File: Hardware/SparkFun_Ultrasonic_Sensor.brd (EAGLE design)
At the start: 45 x 21.5 mm, 51 parts, among them J2 BM04B-SRSS-TB, J3 BM04B-SRSS-TB, Q1 847, U2 STM8L051, U3 TCT40-16T, U4 TCT40-16R, U6 LMV324

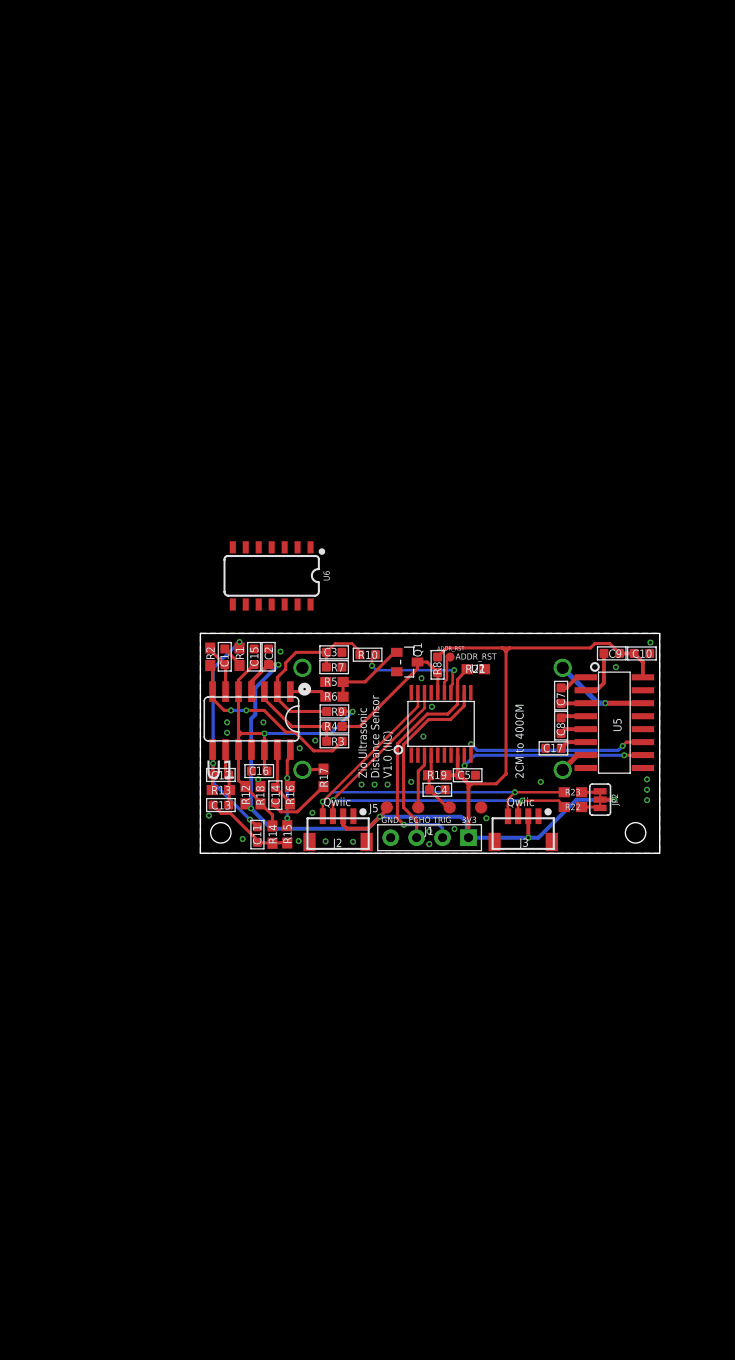
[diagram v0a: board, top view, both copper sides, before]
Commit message: Removes almost any lingering parts from old design. Gets close to finishing schematic
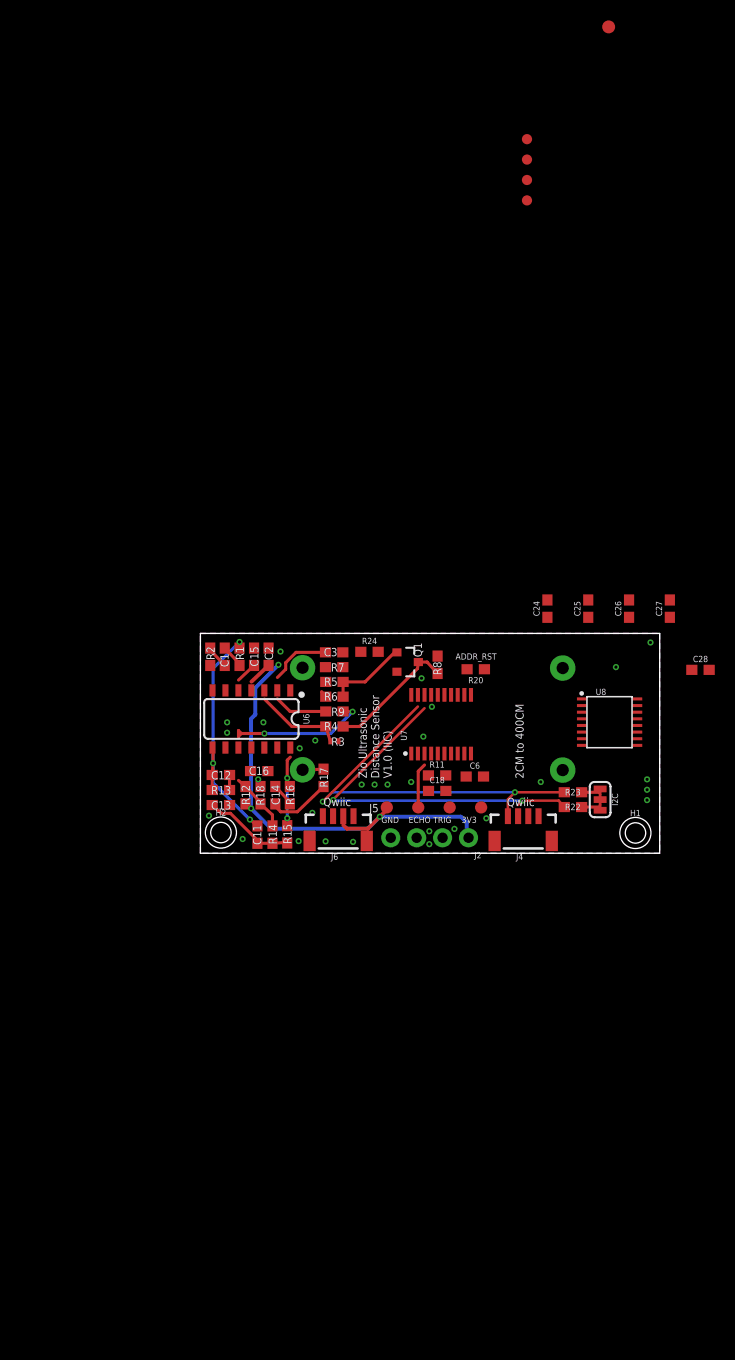
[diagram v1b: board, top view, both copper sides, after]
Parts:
- removed ADDR_RST: (no value), Connector:1P-35MIL
- removed C10, C17, C7, C8, C9: 1uF ±10% 50V, Discretex:0603
- removed C4, C5: 100nF ±10% 50V, Discretex:0603
- removed J1: (no value), Connector:4P-65/35MIL
- removed J3: BM04B-SRSS-TB, Connector:JST-SH-4P-90
- removed JP2: SMT-JUMPER_3_2-NC_TRACE, NOA-Jumpers:SMT-JUMPER_3_2-NC_TRACE
- removed R10: 100K ±1%, Discretex:0603
- removed R19, R21: 10k, SparkFun-Resistors:0603
- removed U1: (no value), IC:SO014
- removed U2: STM8L051, IC:TSSOP20
- removed U3: TCT40-16T, Discretex:TCT40-16T/R
- removed U4: TCT40-16R, Discretex:TCT40-16T/R
- added C18, C24, C25, C26, C27, C28, C6: 0.1uF, SparkFun-Capacitors:0603
- added FD1, FD2, FD3, FD4: FIDUCIAL1X2, SparkFun-Aesthetics:FIDUCIAL-1X2
- added FRAME1: FRAME-LEDGER, SparkFun-Aesthetics:CREATIVE_COMMONS
- added H1, H2: STAND-OFFTIGHT, SparkFun-Hardware:STAND-OFF-TIGHT
- added I2C: JUMPER-SMT_3_2-NC_TRACE_SILK, SparkFun-Jumpers:SMT-JUMPER_3_2-NC_TRACE_SILK
- added J4, J6: Vertical Qwiic Connector, SparkFun-Connectors:JST04_1MM_VERT
- added R11, R20: 10k, SparkFun-Resistors:0603
- added R24: 100k, SparkFun-Resistors:0603
- added TP1: TEST-POINT3X5, SparkFun-Connectors:PAD.03X.05
- added U7: STM8L051F3, new_parts:TSSOP20
- added U8: SP3232EB, new_parts:TSSOP16
- added U9: ULTRASONIC_SENSOR_RECEIVER, new_parts:CUSA-R80
- C1, C14: value 10nF ±10% 50V -> 10nF; device Discretex:0603 -> SparkFun-Capacitors:0603
- C11, C13, C16, C3: value 1nF ±10% 50V -> 1nF; device Discretex:0603 -> SparkFun-Capacitors:0603
- C12: value 68pF ±10% 50V -> 68pF; device Discretex:0603 -> SparkFun-Capacitors:0603
- C15: value 1uF ±10% 50V -> 1.0uF; device Discretex:0603 -> SparkFun-Capacitors:0603
- C2: value 1uF ±1% 50V -> 1.0uF; device Discretex:0603 -> SparkFun-Capacitors:0603
- J2: value BM04B-SRSS-TB -> (none); device Connector:JST-SH-4P-90 -> SparkFun-Connectors:1X04_NO_SILK
- Q1: value 847 -> 600mA/40V; device Discrete:SOT23 -> SparkFun-DiscreteSemi:SOT23-3
- R3: value 4.3K ±1% -> 4.3k; device Discretex:0603 -> SparkFun-Resistors:0402_MURATA
- R4, R9: value 120K ±1% -> 124k; device Discretex:0603 -> SparkFun-Resistors:0603
- R7: value 3.3M ±1% -> 2.2M; device Discretex:0603 -> SparkFun-Resistors:0603
- R8: value 1K ±1% -> 1k; device Discretex:0603 -> SparkFun-Resistors:0603
- U5: value (none) -> ULTRASONIC_SENSOR_TRANSMITTER; device IC:SOIC16 -> new_parts:CUSA-T80
- moved U6 14.2 mm to (5.63, 15.2)
- moved J2 13.0 mm to (26.3, 3.55)
- moved U5 5.07 mm to (35.5, 15.2), flipped to the bottom, turned to 0 degrees
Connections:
- removed net N$11: C15.2, C16.2, R12.1, R14.1, R18.1, R9.1, U1.10, U1.12, U1.5
- removed net N$13: C7.1, U5.3
- removed net N$17: C8.2, U5.4
- removed net N$18: C8.1, U5.5
- removed net N$22: C9.2, U5.2
- removed net N$23: C17.2, U5.6
- removed net N$24: U3.2, U5.14
- removed net N$25: U3.1, U5.7
- removed net N$27: ADDR_RST.P$1, U2.15
- removed net N$28: R10.1, U2.14
- removed net N$42: U2.5
- removed net N$43: U2.6
- removed net N$44: U2.2
- removed net N$45: U2.1
- removed net N$7: C7.2, U5.1
- new net 3.3V: C2.2, C28.1, C6.1, I2C.2, J2.1, J4.2, J6.2, R11.2, R12.2, R8.2, U6.4, U7.P8, U8.P16
- new net ADDR_RST: TP1.1, U7.P15
- new net N: R24.2, U7.P14
- new net N$31: C15.2, C16.2, R12.1, R14.1, R18.1, R9.1, U6.10, U6.12, U6.5
- new net N$37: C25.2, U8.P3
- new net N$38: C24.1, U8.P4
- new net N$39: C24.2, U8.P5
- new net N$40: C27.1, U8.P6
- new net N$41: C26.1, U8.P2
- new net N$48: U5.P1, U8.P14
- new net N$49: U5.P2, U8.P7
- new net N$8: C25.1, U8.P1
- net +3V3: no longer C10.2, C2.2, C5.1, C9.1, J1.1, J2.2, J3.2, JP2.2, R12.2, R19.2, R8.2, U1.4, U2.8, U5.16
- net DIN1: now also U7.P11, U8.P11; no longer U2.10, U5.11
- net DIN2: now also U7.P9, U8.P10; no longer U2.9, U5.10
- net ECHO: now also J2.3, U7.P12; no longer J1.3, U2.12
- net GND: now also C18.2, C26.2, C27.2, C28.2, C6.2, J2.4, J4.1, J6.1, R20.1, U6.11, U7.P7, U8.P15, U9.P2; no longer C10.1, C17.1, C4.1, C5.2, J1.4, J2.1, J2.5, J2.6, J3.1, J3.5, J3.6, R21.2, U1.11, U2.7, U4.2, U5.15
- net INT: now also U7.P16; no longer U2.16
- net N$1: now also R3.P$1, U6.7; no longer R3.1, U1.7
- net N$10: now also U6.8; no longer U1.8
- net N$14: now also U6.14; no longer U1.14
- net N$15: now also U6.13; no longer U1.13
- net N$19: now also I2C.3; no longer JP2.3
- net N$2: now also U6.6; no longer U1.6
- net N$20: now also I2C.1; no longer JP2.1
- net N$26: now also U9.P1; no longer U4.1
- net N$4: now also R3.P$2, U6.3; no longer R3.2, U1.3
- net N$6: now also U6.1; no longer U1.1
- net N$9: now also U6.9; no longer U1.9
- net NRST: now also C18.1, R11.1, U7.P4; no longer C4.2, R19.1, U2.4
- net PB4: now also R24.1, U6.2; no longer R10.2, U1.2
- net SCL: now also J4.4, J6.4, U7.P19; no longer J2.4, J3.4, U2.19
- net SDA: now also J4.3, J6.3, U7.P18; no longer J2.3, J3.3, U2.18
- net SWIM: now also U7.P3; no longer U2.3
- net TRIG: now also J2.2, R20.2, U7.P13; no longer J1.2, R21.1, U2.13
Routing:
- net +3V3: track 120.4 -> 44.6 mm, vias 5 -> 3
- net N$11: track 35.2 -> 0.00 mm, vias 2 -> 0
- net TRIG: track 24.3 -> 0.00 mm, vias 1 -> 0
- net N$31: track 0.00 -> 22.5 mm, vias 0 -> 2
- net DIN2: track 19.0 -> 0.00 mm, vias 2 -> 0
- net N$1: track 18.6 -> 0.00 mm, vias 2 -> 0
- net DIN1: track 18.5 -> 0.00 mm, vias 2 -> 0
- net ECHO: track 18.5 -> 0.00 mm
- net N$28: track 11.8 -> 0.00 mm, vias 2 -> 0
- net N$24: track 9.29 -> 0.00 mm, vias 1 -> 0
- net PB4: track 19.3 -> 11.4 mm
- net NRST: track 6.21 -> 0.24 mm
- net N$22: track 4.98 -> 0.00 mm
- net SDA: track 40.5 -> 36.3 mm
- net N$27: track 3.72 -> 0.00 mm
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
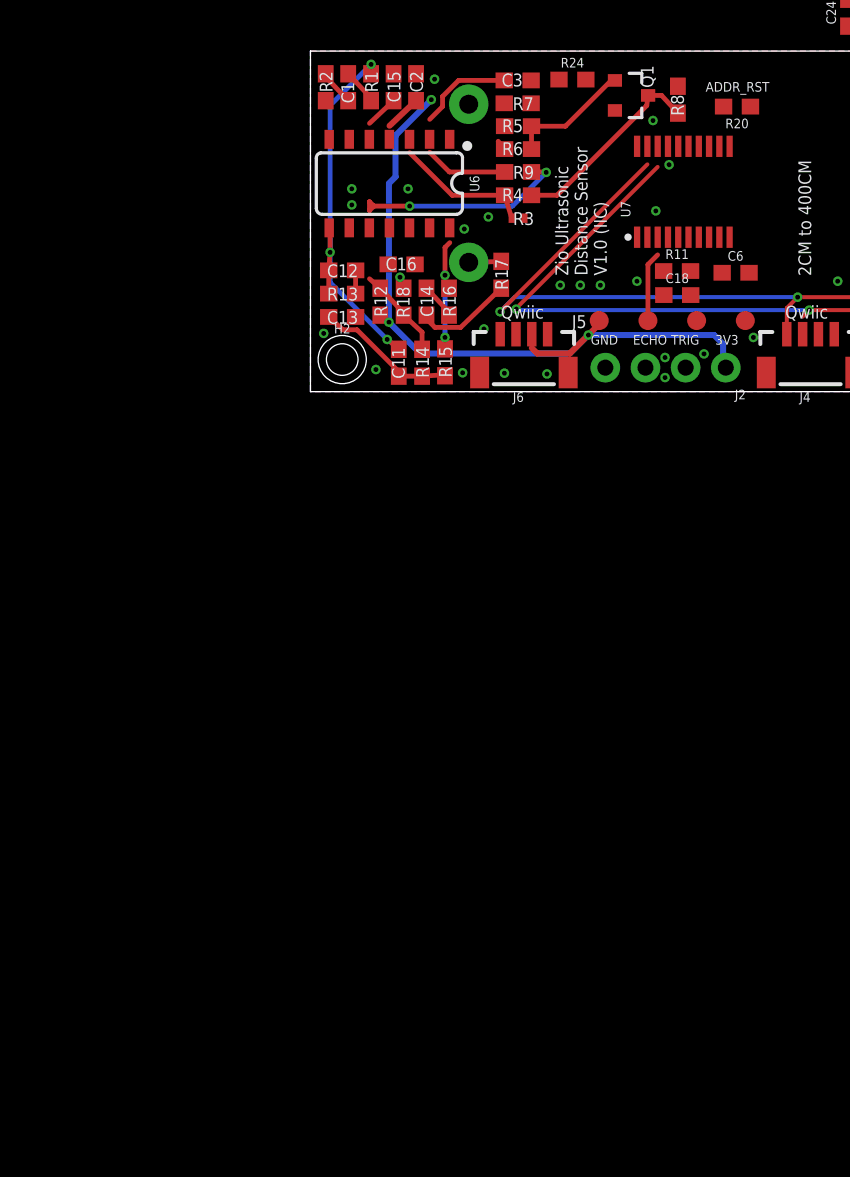
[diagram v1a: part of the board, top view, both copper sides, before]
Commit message: Finishes up schematic
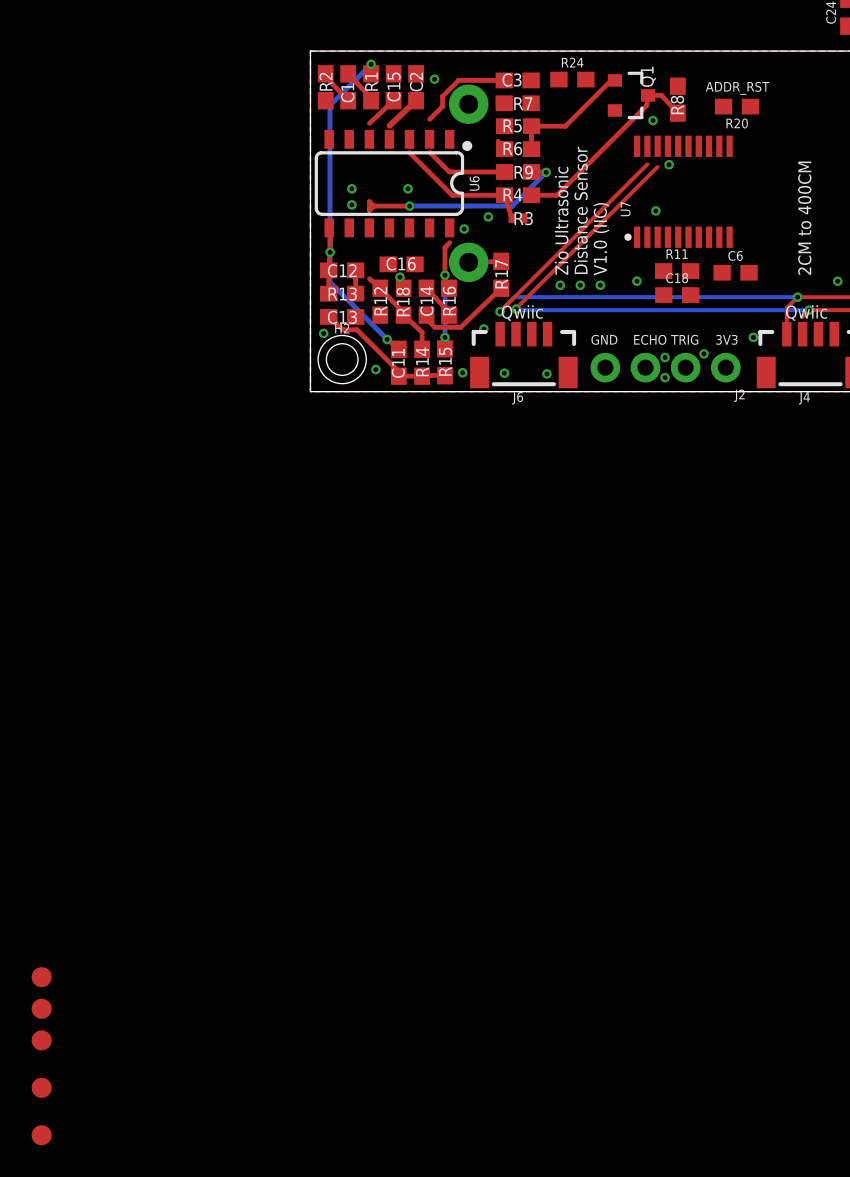
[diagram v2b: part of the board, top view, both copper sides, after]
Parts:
- removed J5: (no value), Connector:TEST_3.08_4P
- added TP2, TP3, TP4, TP5, TP6: TEST-POINT3X5, SparkFun-Connectors:PAD.03X.05
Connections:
- removed net +3V3: J5.4
- net GND: no longer J5.1
- net INT: now also TP6.1
- net NRST: now also TP3.1; no longer J5.2
- net SCL: now also TP5.1
- net SDA: now also TP4.1
- net SWIM: now also TP2.1; no longer J5.3
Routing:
- net +3V3: track 44.6 -> 0.00 mm, vias 3 -> 0
- net SWIM: track 4.41 -> 0.00 mm
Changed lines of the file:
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@@
 <attribute name="VALUE" value="600mA/40V" x="19.6214" y="22.0364" size="0.635" layer="27" ratio="10" rot="R270"/>
-</element>
-<element name="J5" library="Connector" package="TEST_3.08_4P" value="" x="22.8854" y="6.5278" smashed="yes" rot="R180">
-<attribute name="NAME" x="17.4658" y="6.8674" size="0.8128" layer="25" ratio="10" rot="R180"/>
 </element>
 <element name="R22" library="SparkFun-Resistors" package="0603" value="4.7k" x="36.503" y="6.56" smashed="yes">
@@
 <attribute name="VALUE" x="27.54" y="5.582" size="0.6096" layer="27" font="vector" ratio="20" rot="R180"/>
 </element>
+<element name="TP2" library="SparkFun-Connectors" package="PAD.03X.05" value="TEST-POINT3X5" x="-17" y="-35" smashed="yes"/>
+<element name="TP3" library="SparkFun-Connectors" package="PAD.03X.05" value="TEST-POINT3X5" x="-17" y="-37" smashed="yes"/>
+<element name="TP4" library="SparkFun-Connectors" package="PAD.03X.05" value="TEST-POINT3X5" x="-17" y="-39" smashed="yes"/>
+<element name="TP5" library="SparkFun-Connectors" package="PAD.03X.05" value="TEST-POINT3X5" x="-17" y="-42" smashed="yes"/>
+<element name="TP6" library="SparkFun-Connectors" package="PAD.03X.05" value="TEST-POINT3X5" x="-17" y="-45" smashed="yes"/>
 </elements>
 <signals>
@@
 <contactref element="R18" pad="2"/>
 <contactref element="C16" pad="1"/>
-<contactref element="J5" pad="1"/>
 <polygon width="0.2032" layer="1" thermals="no">
 <vertex x="0" y="23.5712"/>
@@
 <wire x1="33.13" y1="5.665" x2="33.3502" y2="9.017" width="0" layer="19" extent="1-1"/>
 <wire x1="28.0162" y1="5.461" x2="33.13" y2="5.665" width="0" layer="19" extent="1-1"/>
-<wire x1="27.5054" y1="6.5278" x2="28.0162" y2="5.461" width="0" layer="19" extent="1-1"/>
-<wire x1="27.74" y1="9.55" x2="27.5054" y2="6.5278" width="0" layer="19" extent="1-1"/>
 <wire x1="24.892" y1="4.4196" x2="28.0162" y2="5.461" width="0" layer="19" extent="1-1"/>
 <wire x1="22.4282" y1="4.191" x2="24.892" y2="4.4196" width="0" layer="19" extent="1-1"/>
 <wire x1="22.4282" y1="2.921" x2="22.4282" y2="4.191" width="0" layer="19" extent="1-1"/>
-<wire x1="24.05" y1="8.14" x2="27.5054" y2="6.5278" width="0" layer="19" extent="1-1"/>
+<wire x1="24.05" y1="8.14" x2="24.892" y2="4.4196" width="0" layer="19" extent="1-1"/>
 <wire x1="20.6502" y1="9.017" x2="24.05" y2="8.14" width="0" layer="19" extent="1-1"/>
 <wire x1="18.3388" y1="8.763" x2="20.6502" y2="9.017" width="0" layer="19" extent="1-1"/>
@@
 <wire x1="19.2564" y1="19.8164" x2="21.6662" y2="19.177" width="0" layer="19" extent="1-1"/>
 <wire x1="18.65" y1="3.55" x2="14.9606" y2="3.1496" width="0" layer="19" extent="1-1"/>
+<wire x1="27.74" y1="9.55" x2="24.562" y2="11.799" width="0" layer="19" extent="1-1"/>
 <wire x1="13.9564" y1="20.2692" x2="19.2564" y2="19.8164" width="0" layer="19" extent="1-1"/>
 <wire x1="13.9564" y1="21.717" x2="13.9564" y2="20.2692" width="0" layer="19" extent="1-1"/>
@@
 <wire x1="23.2604" y1="19.7164" x2="23.241" y2="19.6478" width="0.3048" layer="1"/>
 <contactref element="U7" pad="P16"/>
-<wire x1="23.241" y1="19.6478" x2="23.262" y2="17.549" width="0" layer="19" extent="1-1"/>
+<contactref element="TP6" pad="1"/>
+<wire x1="13.9818" y1="14.4526" x2="-17" y2="-45" width="0" layer="19" extent="1-1"/>
+<wire x1="23.262" y1="17.549" x2="23.241" y2="19.6478" width="0" layer="19" extent="1-1"/>
 </signal>
 <signal name="N$9">
@@
 </signal>
 <signal name="NRST">
-<contactref element="J5" pad="2"/>
-<wire x1="24.4254" y1="6.5278" x2="24.1808" y2="6.5278" width="0.3048" layer="1"/>
 <contactref element="U7" pad="P4"/>
 <contactref element="R11" pad="1"/>
 <contactref element="C18" pad="1"/>
-<wire x1="22.34" y1="9.66" x2="22.612" y2="11.799" width="0" layer="19" extent="1-1"/>
-<wire x1="22.35" y1="8.14" x2="22.34" y2="9.66" width="0" layer="19" extent="1-1"/>
-<wire x1="24.1808" y1="6.5278" x2="22.35" y2="8.14" width="0" layer="19" extent="1-1"/>
+<contactref element="TP3" pad="1"/>
+<wire x1="22.35" y1="8.14" x2="-17" y2="-37" width="0" layer="19" extent="1-1"/>
+<wire x1="22.34" y1="9.66" x2="22.35" y2="8.14" width="0" layer="19" extent="1-1"/>
+<wire x1="22.612" y1="11.799" x2="22.34" y2="9.66" width="0" layer="19" extent="1-1"/>
 </signal>
 <signal name="SWIM">
-<contactref element="J5" pad="3"/>
-<wire x1="21.3454" y1="10.0678" x2="21.3454" y2="6.5278" width="0.3048" layer="1"/>
-<wire x1="21.9604" y1="10.6828" x2="21.3454" y2="10.0678" width="0.3048" layer="1"/>
 <contactref element="U7" pad="P3"/>
-<wire x1="21.9604" y1="10.6828" x2="21.962" y2="11.799" width="0" layer="19" extent="1-1"/>
+<contactref element="TP2" pad="1"/>
+<wire x1="21.962" y1="11.799" x2="-17" y2="-35" width="0" layer="19" extent="1-1"/>
 </signal>
 <signal name="SCL">
@@
 <contactref element="J6" pad="4"/>
 <contactref element="J4" pad="4"/>
-<wire x1="21.3104" y1="16.4082" x2="21.312" y2="17.549" width="0" layer="19" extent="1-1"/>
+<contactref element="TP5" pad="1"/>
+<wire x1="12" y1="5.665" x2="-17" y2="-42" width="0" layer="19" extent="1-1"/>
+<wire x1="12.0006" y1="7.0784" x2="12" y2="5.665" width="0" layer="19" extent="1-1"/>
 <wire x1="30.13" y1="5.665" x2="30.1752" y2="5.72403125" width="0" layer="19" extent="1-1"/>
-<wire x1="12" y1="5.665" x2="12.0006" y2="7.0784" width="0" layer="19" extent="1-1"/>
+<wire x1="21.312" y1="17.549" x2="21.3104" y2="16.4082" width="0" layer="19" extent="1-1"/>
 </signal>
 <signal name="SDA">
@@
 <contactref element="J6" pad="3"/>
 <contactref element="J4" pad="3"/>
-<wire x1="21.9604" y1="16.2454" x2="21.962" y2="17.549" width="0" layer="19" extent="1-1"/>
+<contactref element="TP4" pad="1"/>
+<wire x1="13" y1="5.665" x2="-17" y2="-39" width="0" layer="19" extent="1-1"/>
+<wire x1="13.015253125" y1="7.250946875" x2="13" y2="5.665" width="0" layer="19" extent="1-1"/>
 <wire x1="31.13" y1="5.665" x2="31.1284" y2="6.7698" width="0" layer="19" extent="1-1"/>
-<wire x1="13" y1="5.665" x2="13.015253125" y2="7.250946875" width="0" layer="19" extent="1-1"/>
+<wire x1="21.962" y1="17.549" x2="21.9604" y2="16.2454" width="0" layer="19" extent="1-1"/>
 </signal>
 <signal name="N$19">
@@
 <wire x1="26.512" y1="17.549" x2="42.793" y2="13.903" width="0" layer="19" extent="1-1"/>
 </signal>
-<signal name="+3V3">
-<contactref element="J5" pad="4"/>
-<wire x1="4.953" y1="6.4262" x2="4.9657" y2="6.4262" width="0.381" layer="1"/>
-<via x="4.9657" y="6.4262" extent="1-16" drill="0.3048"/>
-<wire x1="18.2654" y1="6.5278" x2="18.2654" y2="6.302" width="0.381" layer="1"/>
-<wire x1="18.2654" y1="6.302" x2="17.5768" y2="5.6134" width="0.381" layer="1"/>
-<via x="17.5768" y="5.6134" extent="1-16" drill="0.3048"/>
-<wire x1="7.62" y1="20.5232" x2="7.6454" y2="20.4978" width="0.381" layer="1"/>
-<via x="7.6454" y="20.4978" extent="1-16" drill="0.3048"/>
-<wire x1="7.6454" y1="20.4978" x2="5.3848" y2="18.2372" width="0.381" layer="16"/>
-<wire x1="5.3848" y1="15.621" x2="5.3848" y2="18.2372" width="0.381" layer="16"/>
-<wire x1="4.9657" y1="6.4262" x2="4.9657" y2="15.2019" width="0.381" layer="16"/>
-<wire x1="4.9657" y1="15.2019" x2="5.3848" y2="15.621" width="0.381" layer="16"/>
-<wire x1="25.527" y1="5.6134" x2="26.0985" y2="5.0419" width="0.381" layer="16"/>
-<wire x1="25.527" y1="5.6134" x2="17.5768" y2="5.6134" width="0.381" layer="16"/>
-<wire x1="26.0985" y1="5.0419" x2="26.0985" y2="3.7255" width="0.381" layer="16"/>
-<wire x1="14.3462" y1="4.445" x2="14.0006" y2="4.7906" width="0.381" layer="1"/>
-<wire x1="16.4084" y1="4.445" x2="17.5768" y2="5.6134" width="0.381" layer="16"/>
-<wire x1="4.9657" y1="6.4262" x2="6.9469" y2="4.445" width="0.381" layer="16"/>
-<wire x1="6.9469" y1="4.445" x2="16.4084" y2="4.445" width="0.381" layer="16"/>
-<wire x1="17.5768" y1="5.6134" x2="16.4084" y2="4.445" width="0.381" layer="1"/>
-<wire x1="16.4084" y1="4.445" x2="14.3462" y2="4.445" width="0.381" layer="1"/>
-</signal>
 <signal name="N$26">
